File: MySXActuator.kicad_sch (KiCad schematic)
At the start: 23 parts, among them Q1 2N7002, Q2 IRF530, Q3 IRF530, Q4 2N7002, U1 AP63205WU, X1 FE10-2, X2 MKDSN1,5/6-5,08

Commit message: change C2 footprint from 0201 to 0402
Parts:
- C2: footprint Capacitor_SMD:C_0201_0603Metric -> Capacitor_SMD:C_0402_1005Metric
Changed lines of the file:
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@@
       (effects (font (size 1.27 1.27)) (justify left))
     )
-    (property "Footprint" "Capacitor_SMD:C_0201_0603Metric" (at 130.81 65.7352 0)
+    (property "Footprint" "Capacitor_SMD:C_0402_1005Metric" (at 130.81 65.7352 0)
       (effects (font (size 1.27 1.27)) hide)
     )

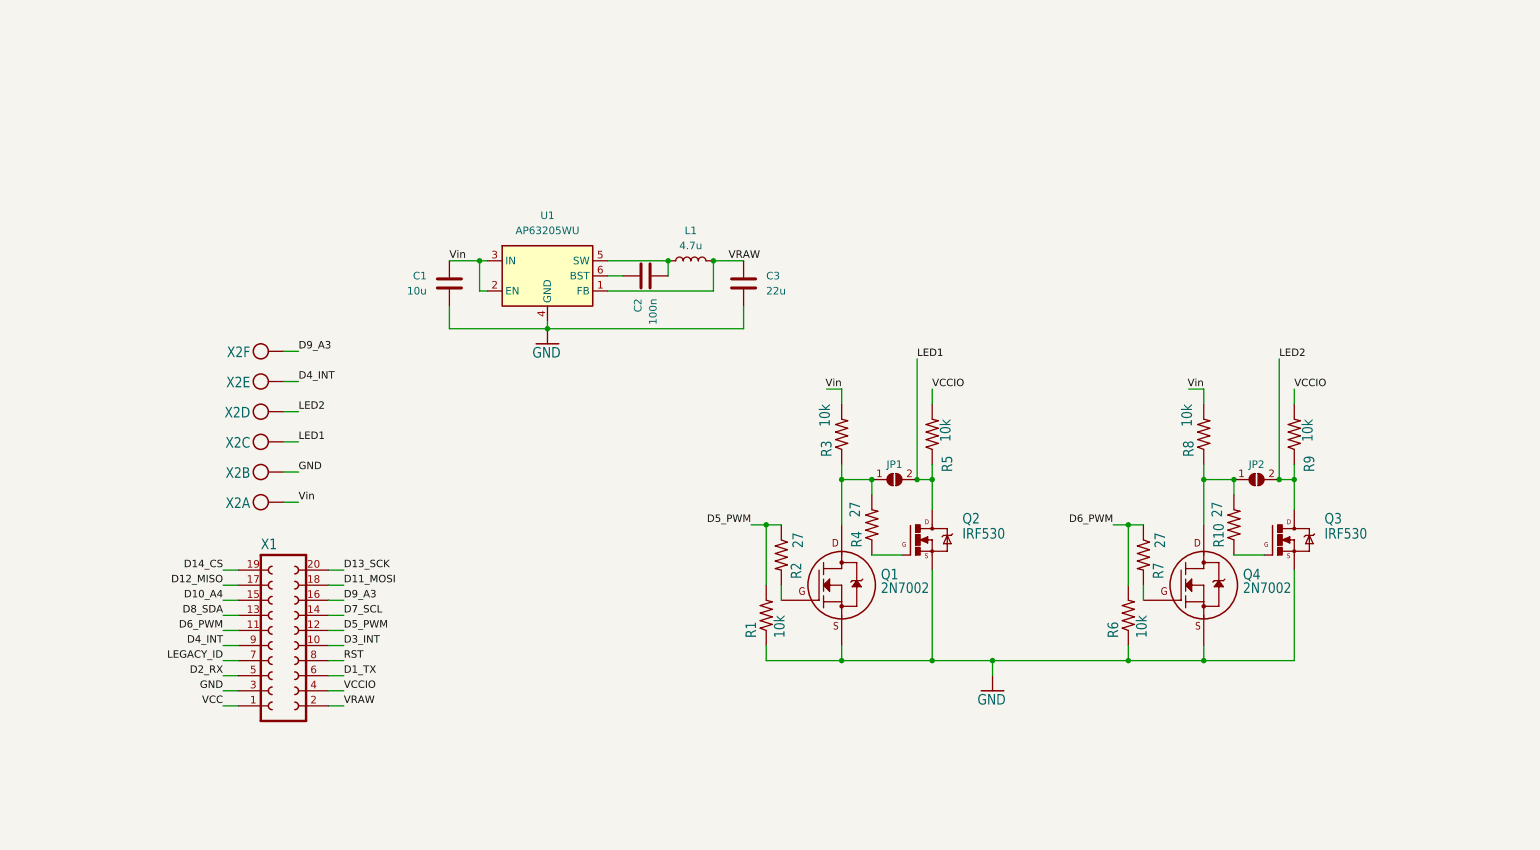
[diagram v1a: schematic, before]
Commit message: refactor schematic to use kicad native symbols and footprints
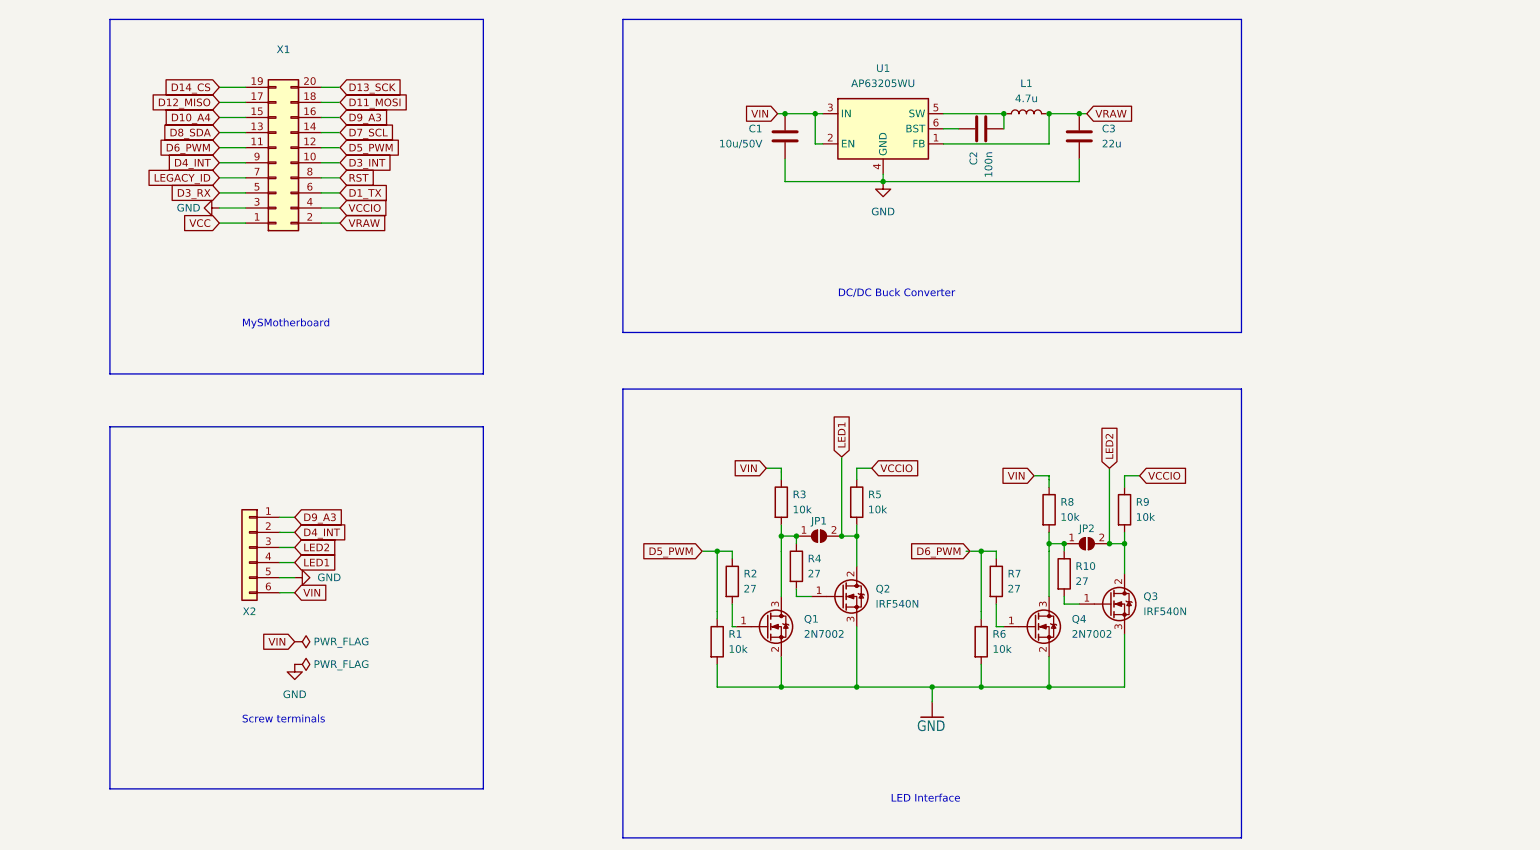
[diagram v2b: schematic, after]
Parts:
- removed Q1, Q4: 2N7002, MySXActuator:SOT-23, symbol MySXActuator-eagle-import:2N700_SOT23
- removed Q2, Q3: IRF530, MySXActuator:TO220BV, symbol MySXActuator-eagle-import:IRF530
- removed R1, R3, R5, R6, R8, R9: 10k, MySXActuator:0603-RES, symbol MySXActuator-eagle-import:RESISTOR0603-RES
- removed R10, R2, R4, R7: 27, MySXActuator:0603-RES, symbol MySXActuator-eagle-import:RESISTOR0603-RES
- removed X1: FE10-2, MySXActuator:FE10-2, symbol MySXActuator-eagle-import:FE10-2
- removed X2: MKDSN1,5/6-5,08, MySXActuator:MKDSN1,5_6-5,08, symbol MySXActuator-eagle-import:MKDSN1,5/6-5,08
- added Q1, Q4: 2N7002, Package_TO_SOT_SMD:SOT-23, symbol Transistor_FET:2N7002
- added Q2, Q3: IRF540N, Package_TO_SOT_THT:TO-220-3_Vertical, symbol Transistor_FET:IRF540N
- added R1, R3, R5, R6, R8, R9: 10k, Resistor_SMD:R_0603_1608Metric, symbol Device:R
- added R10, R2, R4, R7: 27, Resistor_SMD:R_0603_1608Metric, symbol Device:R
- added X1: ~, MySXActuator:FE10-2, symbol Connector_Generic:Conn_02x10_Odd_Even
- added X2: ~, TerminalBlock_Phoenix:TerminalBlock_Phoenix_MKDS-1,5-6-5.08_1x06_P5.08mm_Horizontal, symbol Connector_Generic:Conn_01x06
- C1: value 10u -> 10u/50V
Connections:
- net D10_A4: now also X1.15 (Pin_15)
- net D11_MOSI: now also X1.18 (Pin_18)
- net D12_MISO: now also X1.17 (Pin_17)
- net D13_SCK: now also X1.20 (Pin_20)
- net D14_CS: now also X1.19 (Pin_19)
- net D1_TX: now also X1.6 (Pin_6)
- net D3_INT: now also X1.10 (Pin_10)
- net D4_INT: now also X1.9 (Pin_9), X2.2 (Pin_2)
- net D5_PWM: now also R1.1, R2.1, X1.12 (Pin_12)
- net D6_PWM: now also R6.1, R7.1, X1.11 (Pin_11)
- net D7_SCL: now also X1.14 (Pin_14)
- net D8_SDA: now also X1.13 (Pin_13)
- net D9_A3: now also X1.16 (Pin_16), X2.1 (Pin_1)
- net GND: now also Q1.2 (S), Q2.3 (S), Q3.3 (S), Q4.2 (S), R1.2, R6.2, X1.3 (Pin_3), X2.5 (Pin_5)
- net LED1: now also Q2.2 (D), R5.2, X2.4 (Pin_4)
- net LED2: now also Q3.2 (D), R9.2, X2.3 (Pin_3)
- net LEGACY_ID: now also X1.7 (Pin_7)
- net RST: now also X1.8 (Pin_8)
- net VCC: now also X1.1 (Pin_1)
- net VCCIO: now also R5.1, R9.1, X1.4 (Pin_4)
- net VRAW: now also X1.2 (Pin_2)
- net at JP1.1 (A): now also Q1.3 (D), R3.2, R4.1
- net at JP2.1 (A): now also Q4.3 (D), R10.1, R8.2
- net Vin renamed VIN
- net VIN: now also R3.1, R8.1, X2.6 (Pin_6)
- new net: Q1.1 (G), R2.2
- new net: Q2.1 (G), R4.2
- new net: Q4.1 (G), R7.2
- new net: Q3.1 (G), R10.2
- new net D3_RX: X1.5 (Pin_5)
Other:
- note added: "DC/DC Buck Converter"
- note added: "LED Interface"
- note added: "MySMotherboard"
- note added: "Screw terminals"
- company: (none) -> Marek Czerski
- title: (none) -> MySXActuator
- moved on the sheet: C1, C2, C3, JP1, JP2, L1, U1

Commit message: add reverse polarity protection and overvoltage protection for input pins
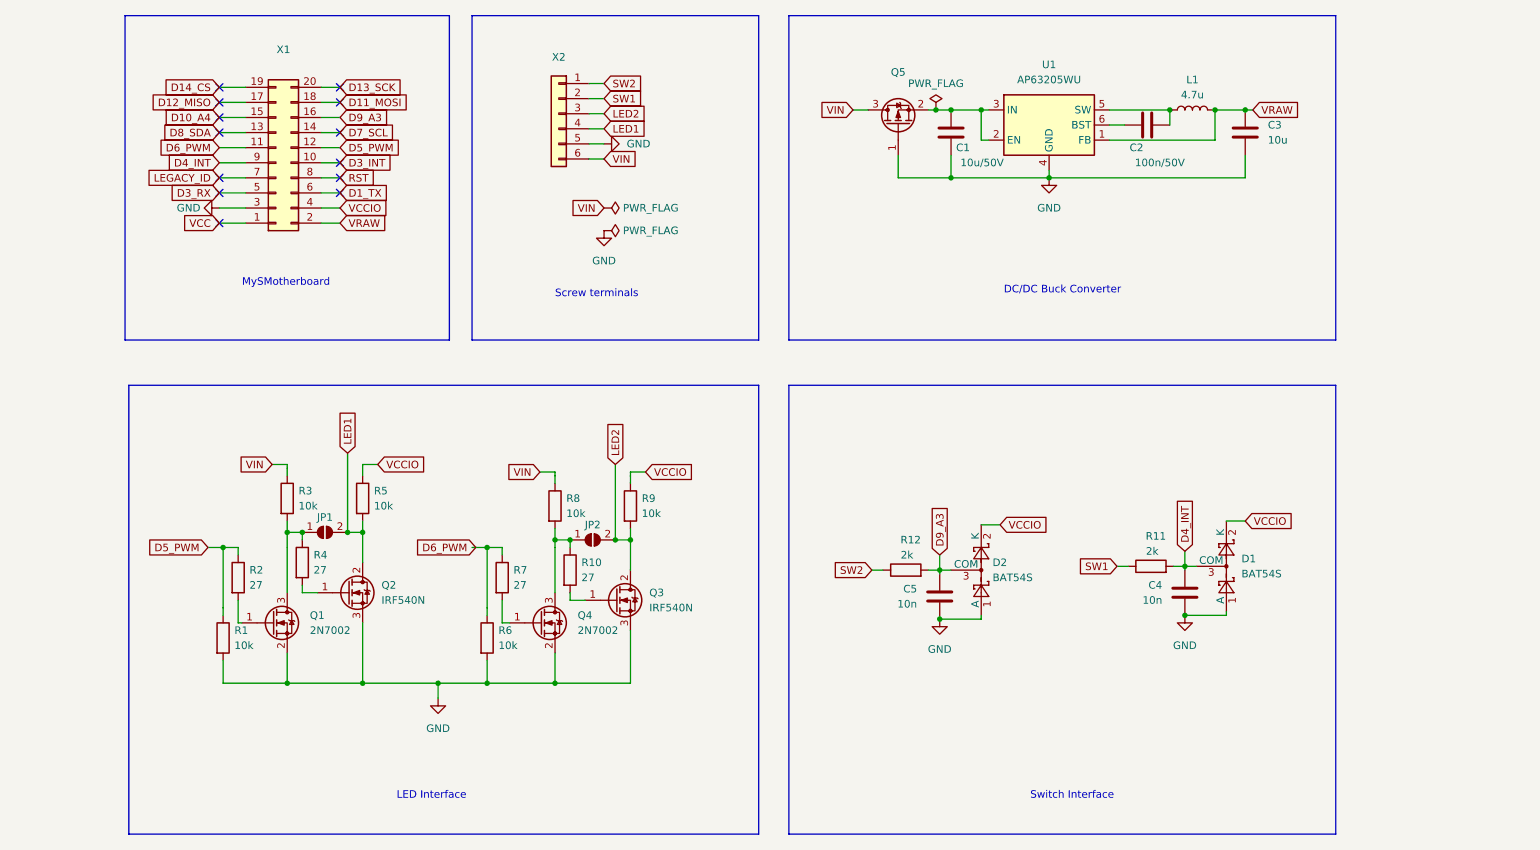
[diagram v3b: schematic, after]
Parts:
- added C4, C5: 10n, Capacitor_SMD:C_0603_1608Metric_Pad1.08x0.95mm_HandSolder, symbol Device:C
- added D1, D2: BAT54S, Package_TO_SOT_SMD:SOT-23, symbol Diode:BAT54S
- added Q5: ~, Package_TO_SOT_SMD:SOT-23, symbol Device:Q_PMOS_GSD
- added R11, R12: 2k, Resistor_SMD:R_0603_1608Metric, symbol Device:R
- C1: footprint Capacitor_SMD:C_1206_3216Metric -> Capacitor_SMD:C_0603_1608Metric_Pad1.08x0.95mm_HandSolder
- C2: value 100n -> 100n/50V; footprint Capacitor_SMD:C_0402_1005Metric -> Capacitor_SMD:C_0402_1005Metric_Pad0.74x0.62mm_HandSolder
- C3: value 22u -> 10u; footprint Capacitor_SMD:C_1206_3216Metric -> Capacitor_SMD:C_0603_1608Metric_Pad1.08x0.95mm_HandSolder
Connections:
- net D4_INT: now also C4.1, D1.3 (COM), R11.2; no longer X2.2 (Pin_2)
- net D9_A3: now also C5.1, D2.3 (COM), R12.2; no longer X2.1 (Pin_1)
- net GND: now also C4.2, C5.2, D1.1 (A), D2.1 (A), Q5.1 (G)
- net VCCIO: now also D1.2 (K), D2.2 (K)
- net VIN: now also Q5.3 (D); no longer C1.1, U1.2 (EN), U1.3 (IN)
- new net: C1.1, Q5.2 (S), U1.2 (EN), U1.3 (IN)
- new net SW1: R11.1, X2.2 (Pin_2)
- new net SW2: R12.1, X2.1 (Pin_1)
- no-connect marks 0 -> 13
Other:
- note added: "Switch Interface"
- moved on the sheet: C1, C2, C3, JP1, JP2, L1, Q1, Q2, Q3, Q4, R1, R10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

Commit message: update schematic
- add zener diode to protect high positive voltage on inputs
- add anoter 2 input sections as alternative to led drivers
- add add rj45 socket for i2c interface
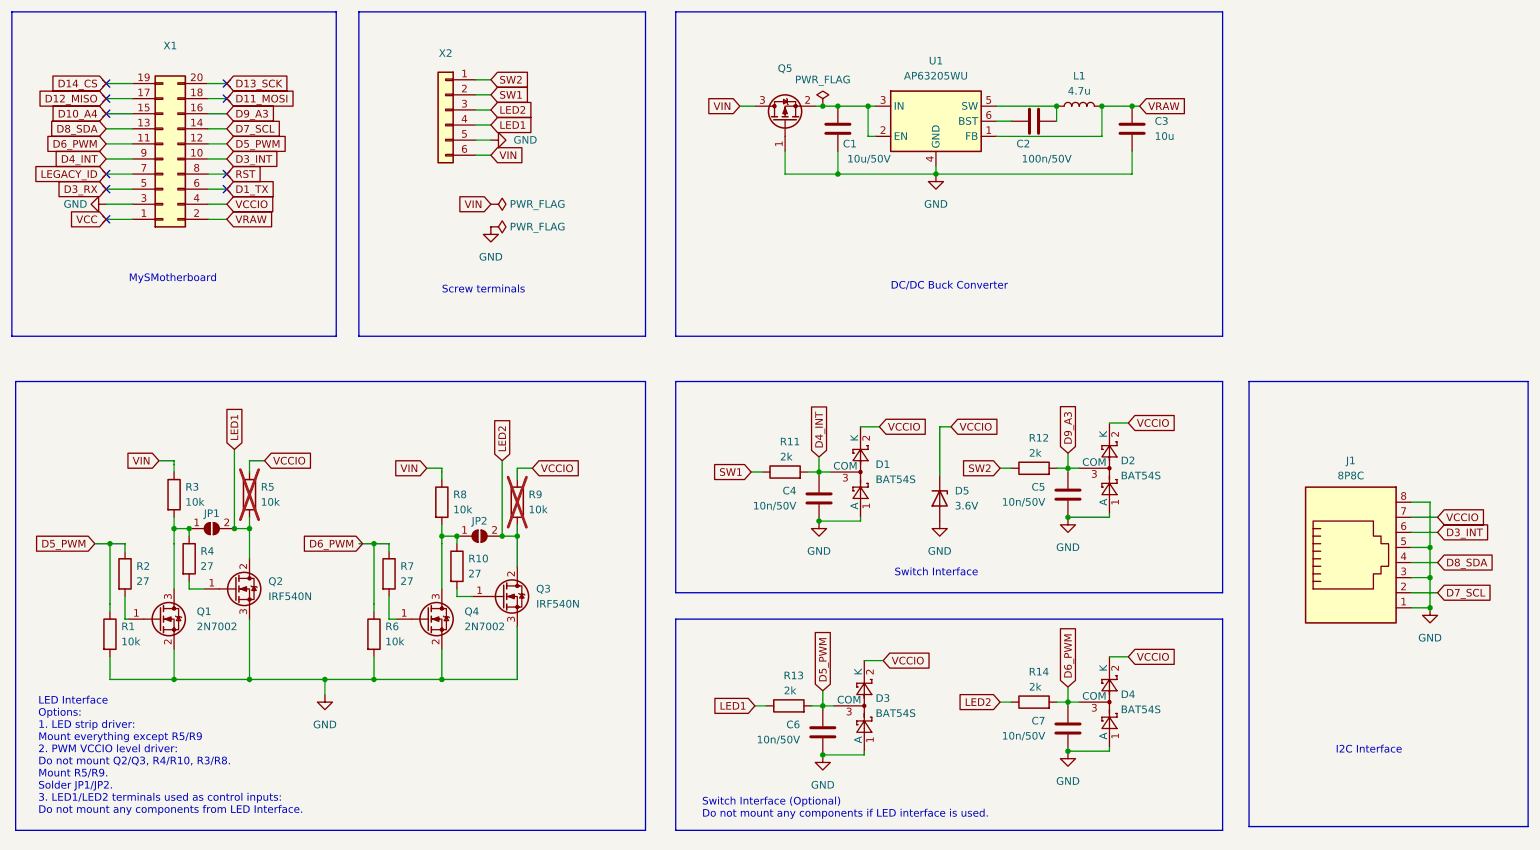
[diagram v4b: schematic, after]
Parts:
- added C6, C7: 10n/50V, Capacitor_SMD:C_0402_1005Metric, symbol Device:C
- added D3, D4: BAT54S, Package_TO_SOT_SMD:SOT-23, symbol Diode:BAT54S
- added D5: 3.6V, Diode_SMD:D_MiniMELF, symbol Device:D_Zener
- added J1: 8P8C, MySXActuator:AMPHENOL_54601-908WPLF, symbol Connector:8P8C
- added R13, R14: 2k, Resistor_SMD:R_0603_1608Metric, symbol Device:R
- C1, C3: footprint Capacitor_SMD:C_0603_1608Metric_Pad1.08x0.95mm_HandSolder -> Capacitor_SMD:C_1206_3216Metric
- C4, C5: value 10n -> 10n/50V; footprint Capacitor_SMD:C_0603_1608Metric_Pad1.08x0.95mm_HandSolder -> Capacitor_SMD:C_0402_1005Metric
- R5, R9: now not fitted
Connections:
- net D3_INT: now also J1.6
- net D5_PWM: now also C6.1, D3.3 (COM), R13.2
- net D6_PWM: now also C7.1, D4.3 (COM), R14.2
- net D7_SCL: now also J1.2
- net D8_SDA: now also J1.4
- net GND: now also C6.2, C7.2, D3.1 (A), D4.1 (A), D5.2 (A), J1.1, J1.3, J1.5, J1.8
- net LED1: now also R13.1
- net LED2: now also R14.1
- net VCCIO: now also D3.2 (K), D4.2 (K), D5.1 (K), J1.7
- no-connect marks 13 -> 10
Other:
- note added: "I2C Interface"
- note added: "LED Interface Options: 1. LED strip driver: Mount everything except R5/R9 2. PWM VCCIO level driver: Do not mount Q2/Q3, R4/R10, R3/R8. Mount R5/R9. Solder JP1/JP2. 3. LED1/LED2 terminals used as control inputs: Do not mount any components from LED Interface."
- note added: "Switch Interface (Optional) Do not mount any components if LED interface is used."
- note removed: "LED Interface"
- moved on the sheet: C1, C2, C3, C4, C5, D1, D2, JP1, JP2, L1, Q1, Q2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

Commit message: update PCB after schematic changes
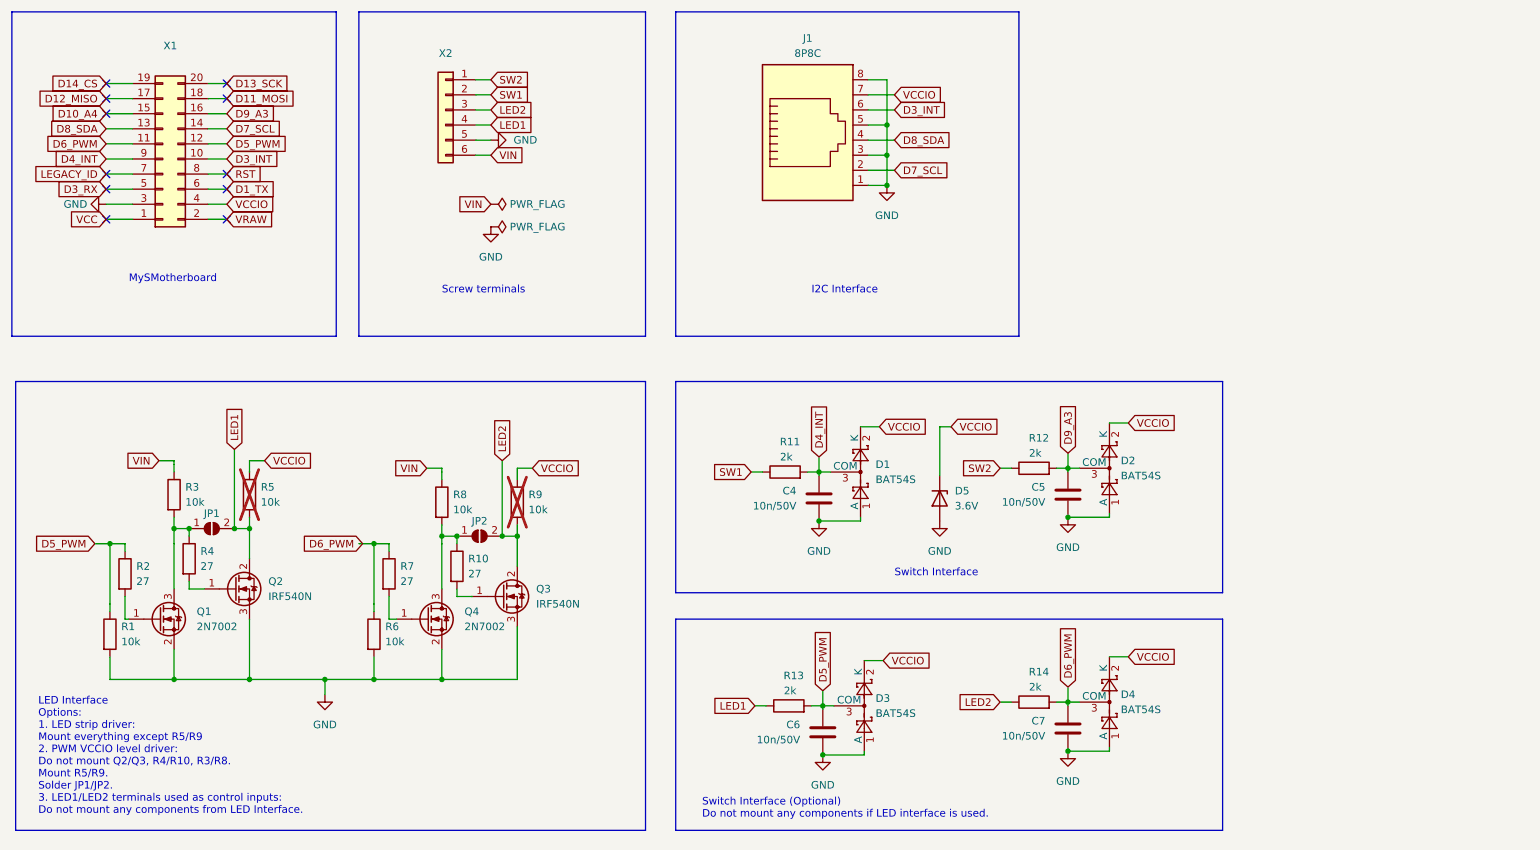
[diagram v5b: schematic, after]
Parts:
- removed C1: 10u/50V, Capacitor_SMD:C_1206_3216Metric, symbol Device:C
- removed C2: 100n/50V, Capacitor_SMD:C_0402_1005Metric_Pad0.74x0.62mm_HandSolder, symbol Device:C
- removed C3: 10u, Capacitor_SMD:C_1206_3216Metric, symbol Device:C
- removed L1: 4.7u, Inductor_SMD:L_1210_3225Metric, symbol Device:L
- removed Q5: ~, Package_TO_SOT_SMD:SOT-23, symbol Device:Q_PMOS_GSD
- removed U1: AP63205WU, Package_TO_SOT_SMD:TSOT-23-6, symbol Regulator_Switching:AP63205WU
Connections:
- no-connect marks 10 -> 11
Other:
- note removed: "DC/DC Buck Converter"
- moved on the sheet: J1
